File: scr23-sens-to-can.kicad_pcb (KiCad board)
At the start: 2 copper layers, 77.2 x 62.5 mm, 66 parts, among them IC1 ADS1256IDBRG4, J2 6473711-1, J3 Conn_ST_STDC14, J4 6437288-2, SW1 SW_SPDT, U1 SRV05-4, U10 AP63205WU, U2 SRV05-4, U3 LM4040DCK-2.5, U4 TJA1042T-3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

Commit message: component
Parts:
- removed U10: AP63205WU, Package_TO_SOT_SMD:TSOT-23-6
- added U7: AP63200WU, Package_TO_SOT_SMD:TSOT-23-6, F.Cu at (113.9, 68.8)
- R5: value 33k -> 34k
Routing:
- net Net-(U7-FB): track 24.7 -> 26.4 mm
- net +12V: track 21.3 -> 21.9 mm

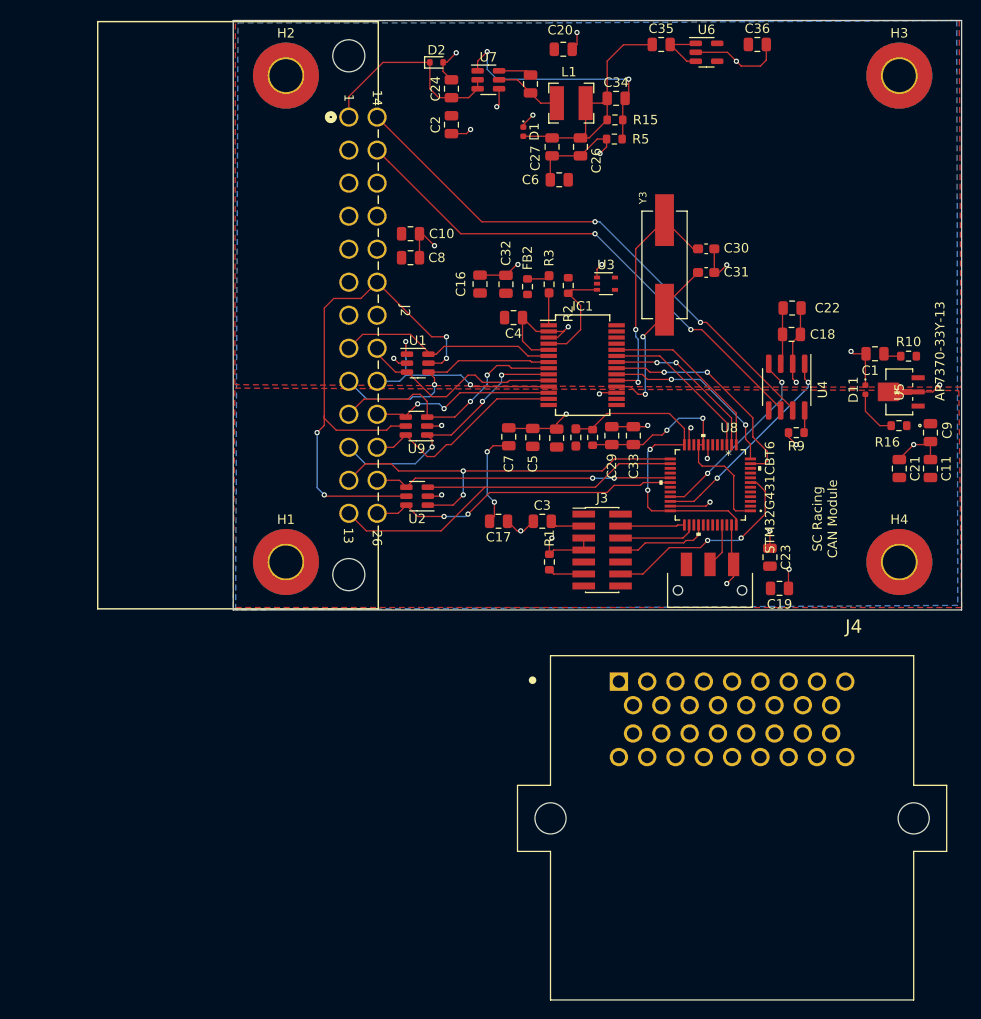
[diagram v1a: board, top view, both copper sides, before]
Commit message: finish traces for new connector
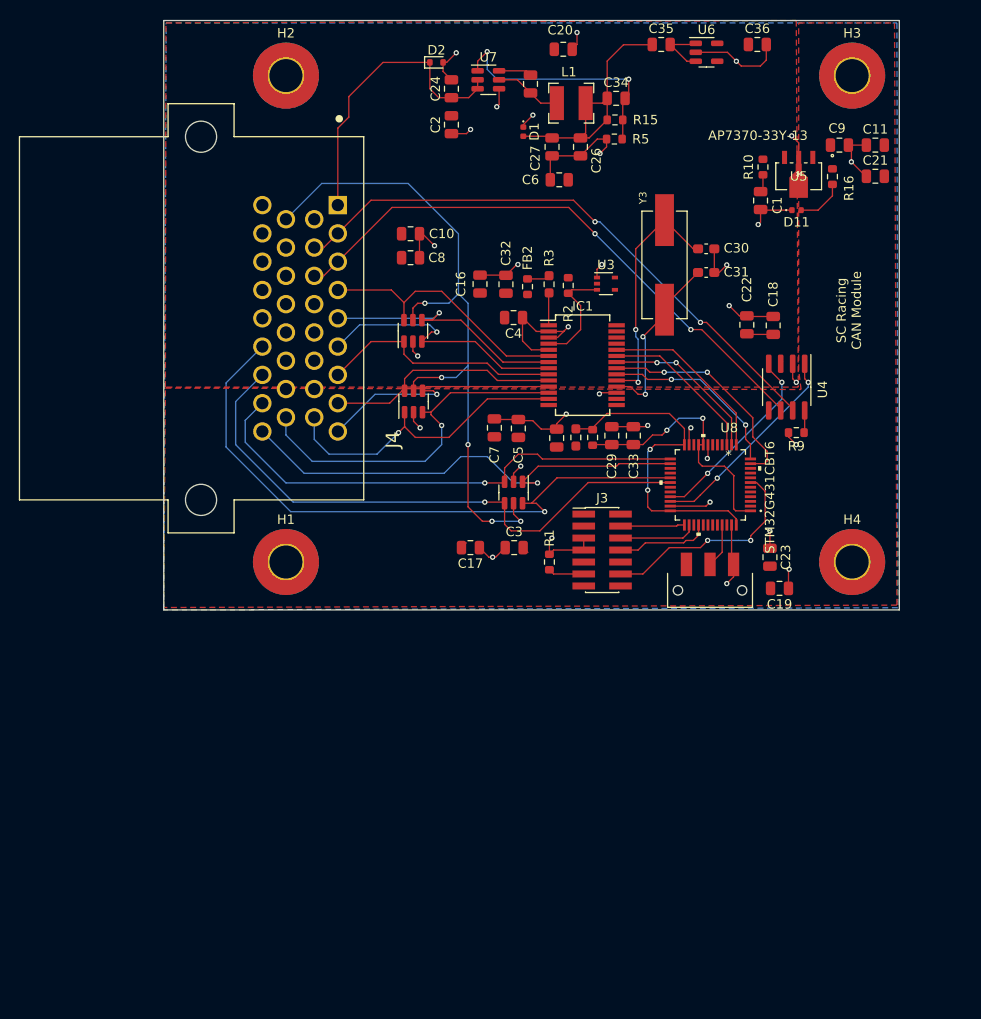
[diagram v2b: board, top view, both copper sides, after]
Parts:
- removed J2: 6473711-1, CON26_2X13_SUPERSEAL_TYC:CON26_2X13_SUPERSEAL_TYC
- moved J4 62.5 mm to (94.0, 94.1), turned to -90 degrees
- moved C11 34.8 mm to (154.9, 75.7), turned to 0 degrees
- moved C9 32.0 mm to (151.1, 75.7), turned to 180 degrees
- moved C21 31.1 mm to (154.9, 79.0), turned to 0 degrees
- moved R16 27.3 mm to (150.4, 79.0), turned to -90 degrees
- moved R10 25.3 mm to (143.0, 78.0), turned to -90 degrees
- moved U5 25.2 mm to (146.8, 79.0), turned to 180 degrees
- moved D11 20.4 mm to (146.6, 82.6), turned to 0 degrees
- moved C1 20.3 mm to (142.8, 81.6), turned to -90 degrees
- moved U2 10.2 mm to (116.6, 112.5), turned to -90 degrees
- moved C22 5.12 mm to (141.3, 94.7), turned to -90 degrees
- moved H3 5.00 mm to (152.5, 68.3)
- moved H4 5.00 mm to (152.5, 119.9)
- moved C17 4.09 mm to (112.0, 118.4)
- moved C3 4.09 mm to (116.7, 118.4)
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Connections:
- J4 pad 1: unconnected-(J4-Pad1) -> +12V
- J4 pad 11: unconnected-(J4-Pad11) -> CANH
- J4 pad 12: unconnected-(J4-Pad12) -> CANL
- J4 pad 13: unconnected-(J4-Pad13) -> GND
- J4 pad 14: unconnected-(J4-Pad14) -> GND
- J4 pad 15: unconnected-(J4-Pad15) -> GND
- J4 pad 17: unconnected-(J4-Pad17) -> A7
- J4 pad 18: unconnected-(J4-Pad18) -> +5V
- J4 pad 2: unconnected-(J4-Pad2) -> CANH
- J4 pad 25: unconnected-(J4-Pad25) -> A6
- J4 pad 3: unconnected-(J4-Pad3) -> CANL
- J4 pad 30: unconnected-(J4-Pad30) -> +5V
- J4 pad 31: unconnected-(J4-Pad31) -> D2
- J4 pad 32: unconnected-(J4-Pad32) -> D3
- J4 pad 33: unconnected-(J4-Pad33) -> D0
- J4 pad 34: unconnected-(J4-Pad34) -> D1
- J4 pad 4: unconnected-(J4-Pad4) -> A0
- J4 pad 5: unconnected-(J4-Pad5) -> A1
- J4 pad 6: unconnected-(J4-Pad6) -> A2
- J4 pad 7: unconnected-(J4-Pad7) -> A3
- J4 pad 8: unconnected-(J4-Pad8) -> A4
- J4 pad 9: unconnected-(J4-Pad9) -> A5
- U1 pad 1: A5 -> A3
- U1 pad 3: A4 -> A2
- U2 pad 1: D0 -> D1
- U2 pad 3: D1 -> D0
- U2 pad 4: D2 -> D3
- U2 pad 6: D3 -> D2
- U9 pad 1: A3 -> A7
- U9 pad 3: A2 -> A6
- U9 pad 4: A6 -> A5
- U9 pad 6: A7 -> A4
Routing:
- net D2: track 31.8 -> 67.4 mm, vias 2 -> 1
- net D3: track 33.4 -> 61.9 mm, vias 2 -> 1
- net A6: track 19.9 -> 38.4 mm, vias 2 -> 1
- net +3.3V: track 14.1 -> 1.44 mm, vias 2 -> 0
- net +5V: track 65.7 -> 77.2 mm, vias 4 -> 5
- net D0: track 42.7 -> 54.1 mm, vias 2 -> 1
- net A7: track 22.2 -> 32.7 mm, vias 0 -> 1
- net +12V: track 21.9 -> 31.7 mm
- net CANL: track 54.3 -> 61.5 mm
- net D1: track 44.1 -> 51.0 mm, vias 0 -> 1
- net CANH: track 57.1 -> 62.1 mm
- net A0: track 23.3 -> 28.1 mm
- net A5: track 24.2 -> 27.4 mm, vias 2 -> 1
- net A4: track 22.2 -> 25.0 mm
- net A1: track 25.8 -> 28.5 mm
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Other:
- board size 77.2 x 62.5 mm -> 78 x 62.5 mm
